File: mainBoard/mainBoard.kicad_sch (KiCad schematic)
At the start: 15 parts, among them J1 Conn_01x04, J2 Conn_01x04, J6 Conn_01x07, J7 Conn_01x07

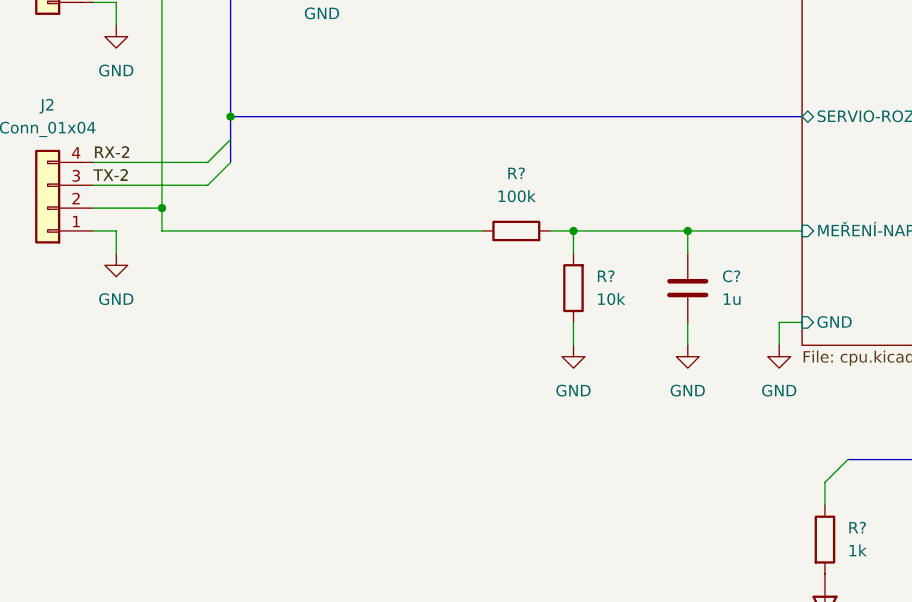
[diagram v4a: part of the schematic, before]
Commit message: test-point na děliči
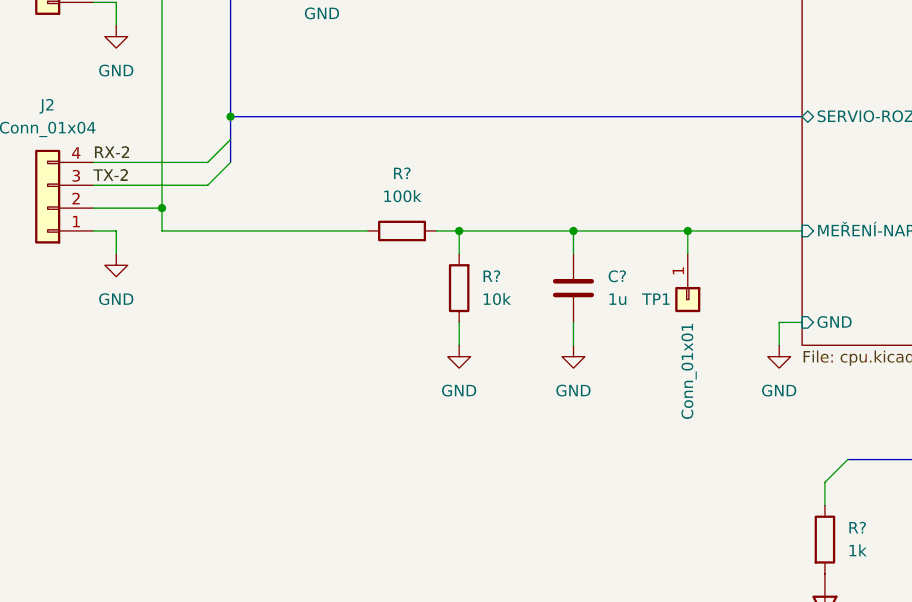
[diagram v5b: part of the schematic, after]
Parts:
- added TP1: Conn_01x01, Connector_Pin:Pin_D0.7mm_L6.5mm_W1.8mm_FlatFork, symbol Connector_Generic:Conn_01x01
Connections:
- net CPU/MEŘENÍ-NAPÁJENÍ: now also TP1.1 (Pin_1)
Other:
- moved on the sheet: C?, R?
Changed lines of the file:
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@@
   (junction (at 63.5 88.9) (diameter 0) (color 0 0 0 0)
   )
+  (junction (at 101.6 101.6) (diameter 0) (color 0 0 0 0)
+  )
   (junction (at 55.88 66.04) (diameter 0) (color 255 0 0 1)
   )
@@
   (junction (at 114.3 101.6) (diameter 0) (color 0 0 0 0)
   )
-  (junction (at 101.6 101.6) (diameter 0) (color 0 0 0 0)
+  (junction (at 88.9 101.6) (diameter 0) (color 0 0 0 0)
   )
   (bus_entry (at 60.96 93.98) (size 2.54 -2.54)
@@
     (stroke (width 0) (type default))
   )
-  (wire (pts (xy 114.3 101.6) (xy 127 101.6))
-    (stroke (width 0) (type default))
-  )
-  (wire (pts (xy 99.06 101.6) (xy 101.6 101.6))
+  (wire (pts (xy 86.36 101.6) (xy 88.9 101.6))
     (stroke (width 0) (type default))
   )
@@
     (stroke (width 0) (type default))
   )
+  (wire (pts (xy 114.3 101.6) (xy 114.3 104.14))
+    (stroke (width 0) (type default))
+  )
   (bus (pts (xy 203.2 38.1) (xy 203.2 60.96))
     (stroke (width 0) (type default))
@@
     (stroke (width 0) (type default))
   )
-  (wire (pts (xy 101.6 111.76) (xy 101.6 114.3))
+  (wire (pts (xy 88.9 111.76) (xy 88.9 114.3))
     (stroke (width 0) (type default))
   )
@@
     (stroke (width 0) (type default))
   )
-  (wire (pts (xy 101.6 101.6) (xy 101.6 104.14))
-    (stroke (width 0) (type default))
-  )
-  (wire (pts (xy 101.6 101.6) (xy 114.3 101.6))
+  (wire (pts (xy 88.9 101.6) (xy 88.9 104.14))
+    (stroke (width 0) (type default))
+  )
+  (wire (pts (xy 88.9 101.6) (xy 101.6 101.6))
     (stroke (width 0) (type default))
   )
@@
     (stroke (width 0) (type default))
   )
-  (wire (pts (xy 114.3 104.14) (xy 114.3 101.6))
+  (wire (pts (xy 101.6 104.14) (xy 101.6 101.6))
     (stroke (width 0) (type default))
   )
@@
     (stroke (width 0) (type default) (color 255 0 0 1))
   )
+  (wire (pts (xy 114.3 101.6) (xy 127 101.6))
+    (stroke (width 0) (type default))
+  )
   (bus (pts (xy 203.2 66.04) (xy 203.2 68.58))
     (stroke (width 0) (type default))
@@
   )
   (wire (pts (xy 48.26 96.52) (xy 60.96 96.52))
+    (stroke (width 0) (type default))
+  )
+  (wire (pts (xy 101.6 101.6) (xy 114.3 101.6))
     (stroke (width 0) (type default))
   )
@@
     (stroke (width 0) (type default))
   )
-  (wire (pts (xy 114.3 111.76) (xy 114.3 114.3))
+  (wire (pts (xy 101.6 111.76) (xy 101.6 114.3))
     (stroke (width 0) (type default))
   )
@@
     (stroke (width 0.3) (type default) (color 0 0 0 1))
   )
-  (wire (pts (xy 91.44 101.6) (xy 55.88 101.6))
+  (wire (pts (xy 78.74 101.6) (xy 55.88 101.6))
     (stroke (width 0) (type default) (color 255 0 0 1))
   )
@@
     )
   )
-  (symbol (lib_id "Device:R") (at 101.6 107.95 180) (unit 1)
-    (in_bom yes) (on_board yes) (dnp no) (fields_autoplaced)
-    (property "Reference" "R?" (at 104.14 106.68 0)
+  (symbol (lib_id "Device:R") (at 88.9 107.95 180) (unit 1)
+    (in_bom yes) (on_board yes) (dnp no) (fields_autoplaced)
+    (property "Reference" "R?" (at 91.44 106.68 0)
       (effects (font (size 1.27 1.27)) (justify right))
     )
-    (property "Value" "10k" (at 104.14 109.22 0)
+    (property "Value" "10k" (at 91.44 109.22 0)
       (effects (font (size 1.27 1.27)) (justify right))
     )
-    (property "Footprint" "Capacitor_SMD:C_0402_1005Metric" (at 103.378 107.95 90)
-      (effects (font (size 1.27 1.27)) hide)
-    )
-    (property "Datasheet" "~" (at 101.6 107.95 0)
-      (effects (font (size 1.27 1.27)) hide)
-    )
-    (property "LCSC" "C25744" (at 101.6 107.95 0)
+    (property "Footprint" "Capacitor_SMD:C_0402_1005Metric" (at 90.678 107.95 90)
+      (effects (font (size 1.27 1.27)) hide)
+    )
+    (property "Datasheet" "~" (at 88.9 107.95 0)
+      (effects (font (size 1.27 1.27)) hide)
+    )
+    (property "LCSC" "C25744" (at 88.9 107.95 0)
       (effects (font (size 1.27 1.27)) hide)
     )
@@
     )
   )
-  (symbol (lib_id "power:GND") (at 101.6 114.3 0) (unit 1)
-    (in_bom yes) (on_board yes) (dnp no) (fields_autoplaced)
-    (property "Reference" "#PWR04" (at 101.6 120.65 0)
-      (effects (font (size 1.27 1.27)) hide)
-    )
-    (property "Value" "GND" (at 101.6 119.38 0)
-      (effects (font (size 1.27 1.27)))
-    )
-    (property "Footprint" "" (at 101.6 114.3 0)
-      (effects (font (size 1.27 1.27)) hide)
-    )
-    (property "Datasheet" "" (at 101.6 114.3 0)
+  (symbol (lib_id "power:GND") (at 88.9 114.3 0) (unit 1)
+    (in_bom yes) (on_board yes) (dnp no) (fields_autoplaced)
+    (property "Reference" "#PWR04" (at 88.9 120.65 0)
+      (effects (font (size 1.27 1.27)) hide)
+    )
+    (property "Value" "GND" (at 88.9 119.38 0)
+      (effects (font (size 1.27 1.27)))
+    )
+    (property "Footprint" "" (at 88.9 114.3 0)
+      (effects (font (size 1.27 1.27)) hide)
+    )
+    (property "Datasheet" "" (at 88.9 114.3 0)
       (effects (font (size 1.27 1.27)) hide)
     )
@@
     )
   )
-  (symbol (lib_id "Device:R") (at 95.25 101.6 90) (unit 1)
-    (in_bom yes) (on_board yes) (dnp no) (fields_autoplaced)
-    (property "Reference" "R?" (at 95.25 95.25 90)
-      (effects (font (size 1.27 1.27)))
-    )
-    (property "Value" "100k" (at 95.25 97.79 90)
-      (effects (font (size 1.27 1.27)))
-    )
-    (property "Footprint" "Capacitor_SMD:C_0402_1005Metric" (at 95.25 103.378 90)
-      (effects (font (size 1.27 1.27)) hide)
-    )
-    (property "Datasheet" "~" (at 95.25 101.6 0)
-      (effects (font (size 1.27 1.27)) hide)
-    )
-    (property "LCSC" "C25741" (at 95.25 101.6 0)
+  (symbol (lib_id "Device:R") (at 82.55 101.6 90) (unit 1)
+    (in_bom yes) (on_board yes) (dnp no) (fields_autoplaced)
+    (property "Reference" "R?" (at 82.55 95.25 90)
+      (effects (font (size 1.27 1.27)))
+    )
+    (property "Value" "100k" (at 82.55 97.79 90)
+      (effects (font (size 1.27 1.27)))
+    )
+    (property "Footprint" "Capacitor_SMD:C_0402_1005Metric" (at 82.55 103.378 90)
+      (effects (font (size 1.27 1.27)) hide)
+    )
+    (property "Datasheet" "~" (at 82.55 101.6 0)
+      (effects (font (size 1.27 1.27)) hide)
+    )
+    (property "LCSC" "C25741" (at 82.55 101.6 0)
       (effects (font (size 1.27 1.27)) hide)
     )
@@
     )
   )
-  (symbol (lib_id "Device:C") (at 114.3 107.95 0) (unit 1)
+  (symbol (lib_id "Device:C") (at 101.6 107.95 0) (unit 1)
     (in_bom yes) (on_board yes) (dnp no)
-    (property "Reference" "C?" (at 118.11 106.68 0)
+    (property "Reference" "C?" (at 105.41 106.68 0)
       (effects (font (size 1.27 1.27)) (justify left))
     )
-    (property "Value" "1u" (at 118.11 109.22 0)
+    (property "Value" "1u" (at 105.41 109.22 0)
       (effects (font (size 1.27 1.27)) (justify left))
     )
-    (property "Footprint" "Capacitor_SMD:C_0402_1005Metric" (at 115.2652 111.76 0)
-      (effects (font (size 1.27 1.27)) hide)
-    )
-    (property "Datasheet" "~" (at 114.3 107.95 0)
-      (effects (font (size 1.27 1.27)) hide)
-    )
-    (property "LCSC" "C52923" (at 114.3 107.95 0)
+    (property "Footprint" "Capacitor_SMD:C_0402_1005Metric" (at 102.5652 111.76 0)
+      (effects (font (size 1.27 1.27)) hide)
+    )
+    (property "Datasheet" "~" (at 101.6 107.95 0)
+      (effects (font (size 1.27 1.27)) hide)
+    )
+    (property "LCSC" "C52923" (at 101.6 107.95 0)
       (effects (font (size 1.27 1.27)) hide)
     )
@@
     )
   )
-  (symbol (lib_id "power:GND") (at 114.3 114.3 0) (unit 1)
-    (in_bom yes) (on_board yes) (dnp no) (fields_autoplaced)
-    (property "Reference" "#PWR03" (at 114.3 120.65 0)
-      (effects (font (size 1.27 1.27)) hide)
-    )
-    (property "Value" "GND" (at 114.3 119.38 0)
-      (effects (font (size 1.27 1.27)))
-    )
-    (property "Footprint" "" (at 114.3 114.3 0)
-      (effects (font (size 1.27 1.27)) hide)
-    )
-    (property "Datasheet" "" (at 114.3 114.3 0)
+  (symbol (lib_id "power:GND") (at 101.6 114.3 0) (unit 1)
+    (in_bom yes) (on_board yes) (dnp no) (fields_autoplaced)
+    (property "Reference" "#PWR03" (at 101.6 120.65 0)
+      (effects (font (size 1.27 1.27)) hide)
+    )
+    (property "Value" "GND" (at 101.6 119.38 0)
+      (effects (font (size 1.27 1.27)))
+    )
+    (property "Footprint" "" (at 101.6 114.3 0)
+      (effects (font (size 1.27 1.27)) hide)
+    )
+    (property "Datasheet" "" (at 101.6 114.3 0)
       (effects (font (size 1.27 1.27)) hide)
     )
@@
         )
       )
+    )
+  )
+  (symbol (lib_id "Connector_Generic:Conn_01x01") (at 114.3 109.22 270) (unit 1)
+    (in_bom yes) (on_board yes) (dnp no)
+    (property "Reference" "TP1" (at 109.22 109.22 90)
+      (effects (font (size 1.27 1.27)) (justify left))
+    )
+    (property "Value" "Conn_01x01" (at 114.3 111.76 0)
+      (effects (font (size 1.27 1.27)) (justify left))
+    )
+    (property "Footprint" "Connector_Pin:Pin_D0.7mm_L6.5mm_W1.8mm_FlatFork" (at 114.3 109.22 0)
+      (effects (font (size 1.27 1.27)) hide)
+    )
+    (property "Datasheet" "~" (at 114.3 109.22 0)
+      (effects (font (size 1.27 1.27)) hide)
+    )
+    (pin "1")
+    (instances
+      (project "mainBoard"
+        (path "/30ed06d7-0b03-4878-b461-066cda7e7438/007b5876-baf1-4b85-a507-5fa12bfe2ac5"
+          (reference "TP1") (unit 1)
+        )
+        (path "/30ed06d7-0b03-4878-b461-066cda7e7438"
+          (reference "TP3") (unit 1)
+        )
+      )

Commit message: test-pointy na ENC-POT
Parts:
- added TP1: Conn_01x01, Connector_Pin:Pin_D0.7mm_L6.5mm_W1.8mm_FlatFork, symbol Connector_Generic:Conn_01x01
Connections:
- net ENC-POT: now also TP1.1 (Pin_1)
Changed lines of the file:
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@@
 (kicad_sch (version 20230121) (generator eeschema)
   (paper "A4")
+  (junction (at 214.63 25.4) (diameter 0) (color 0 0 0 0)
+  )
   (junction (at 55.88 73.66) (diameter 0) (color 255 0 0 1)
   )
@@
     (stroke (width 0) (type default) (color 255 0 0 1))
   )
+  (wire (pts (xy 214.63 25.4) (xy 224.79 25.4))
+    (stroke (width 0) (type default))
+  )
   (wire (pts (xy 73.66 69.85) (xy 76.2 69.85))
     (stroke (width 0.3) (type default) (color 0 0 0 1))
@@
     (stroke (width 0.3) (type default) (color 0 0 0 1))
   )
-  (wire (pts (xy 205.74 25.4) (xy 224.79 25.4))
+  (wire (pts (xy 205.74 25.4) (xy 214.63 25.4))
     (stroke (width 0) (type default))
   )
@@
     (stroke (width 0) (type default) (color 255 0 0 1))
   )
+  (wire (pts (xy 214.63 19.05) (xy 214.63 25.4))
+    (stroke (width 0) (type default))
+  )
   (bus (pts (xy 203.2 30.48) (xy 203.2 33.02))
     (stroke (width 0) (type default))
@@
   (wire (pts (xy 222.25 40.64) (xy 224.79 40.64))
     (stroke (width 0.3) (type default) (color 0 0 0 1))
+  )
+  (wire (pts (xy 214.63 19.05) (xy 224.79 19.05))
+    (stroke (width 0) (type default))
   )
   (wire (pts (xy 129.54 129.54) (xy 129.54 132.08))
@@
         )
       )
+    )
+  )
+  (symbol (lib_id "Connector_Generic:Conn_01x01") (at 229.87 19.05 0) (unit 1)
+    (in_bom yes) (on_board yes) (dnp no)
+    (property "Reference" "TP1" (at 228.6 15.24 0)
+      (effects (font (size 1.27 1.27)) (justify left))
+    )
+    (property "Value" "Conn_01x01" (at 232.41 19.05 0)
+      (effects (font (size 1.27 1.27)) (justify left))
+    )
+    (property "Footprint" "Connector_Pin:Pin_D0.7mm_L6.5mm_W1.8mm_FlatFork" (at 229.87 19.05 0)
+      (effects (font (size 1.27 1.27)) hide)
+    )
+    (property "Datasheet" "~" (at 229.87 19.05 0)
+      (effects (font (size 1.27 1.27)) hide)
+    )
+    (pin "1")
+    (instances
+      (project "mainBoard"
+        (path "/30ed06d7-0b03-4878-b461-066cda7e7438/007b5876-baf1-4b85-a507-5fa12bfe2ac5"
+          (reference "TP1") (unit 1)
+        )
+        (path "/30ed06d7-0b03-4878-b461-066cda7e7438"
+          (reference "TP4") (unit 1)
+        )
+      )

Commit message: WIP
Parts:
- removed R?: 1k, Capacitor_SMD:C_0402_1005Metric, symbol Device:R
- J7: footprint Connector_PinHeader_1.00mm:PinHeader_1x07_P1.00mm_Horizontal -> Connector_PinHeader_1.00mm:PinHeader_1x07_P1.00mm_Vertical
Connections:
- net GND: now also R?.2, R?.2; no longer D1.1 (K), D2.1 (K), D3.1 (K)
- net at D2.2 (A): no longer R?.2
- net at R?.1: now also D1.1 (K), D3.1 (K)
- net at D1.2 (A): no longer R?.2
- net at R?.1: now also D2.1 (K)
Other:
- note removed: "SERVIO-ROZHRANÍ"
- moved on the sheet: C?, D1, D2, D3, D4, J1, J2, J6, J7, R?, TP1

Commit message: WIP
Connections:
- net LED-B: now reaches D3.2 (A)
- net LED-Y: now reaches R?.1
- net LED-G: now reaches D2.2 (A)
- net LED-R: now reaches D1.2 (A)
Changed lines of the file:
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@@
   (junction (at 214.63 30.48) (diameter 0) (color 0 0 0 0)
+  )
+  (junction (at 55.88 91.44) (diameter 0) (color 255 0 0 1)
   )
   (junction (at 129.54 147.32) (diameter 0) (color 0 0 0 0)
@@
     (stroke (width 0) (type default))
   )
+  (wire (pts (xy 55.88 91.44) (xy 55.88 104.14))
+    (stroke (width 0) (type default) (color 255 0 0 1))
+  )
   (bus (pts (xy 63.5 88.9) (xy 63.5 96.52))
     (stroke (width 0) (type default))
@@
     (stroke (width 0.3) (type default) (color 0 0 0 1))
   )
-  (wire (pts (xy 55.88 81.28) (xy 55.88 104.14))
+  (wire (pts (xy 205.74 38.1) (xy 224.79 38.1))
+    (stroke (width 0) (type default))
+  )
+  (wire (pts (xy 129.54 147.32) (xy 129.54 144.78))
+    (stroke (width 0) (type default))
+  )
+  (wire (pts (xy 48.26 99.06) (xy 60.96 99.06))
+    (stroke (width 0) (type default))
+  )
+  (wire (pts (xy 55.88 81.28) (xy 55.88 91.44))
     (stroke (width 0) (type default) (color 255 0 0 1))
-  )
-  (wire (pts (xy 205.74 38.1) (xy 224.79 38.1))
-    (stroke (width 0) (type default))
-  )
-  (wire (pts (xy 129.54 147.32) (xy 129.54 144.78))
-    (stroke (width 0) (type default))
-  )
-  (wire (pts (xy 48.26 99.06) (xy 60.96 99.06))
-    (stroke (width 0) (type default))
-  )
-  (bus (pts (xy 177.8 106.68) (xy 190.5 106.68))
-    (stroke (width 0) (type default))
   )
   (wire (pts (xy 88.9 106.68) (xy 88.9 109.22))
@@
     (stroke (width 0) (type default))
   )
+  (bus (pts (xy 177.8 106.68) (xy 190.5 106.68))
+    (stroke (width 0) (type default))
+  )
   (bus (pts (xy 203.2 71.12) (xy 203.2 73.66))
     (stroke (width 0) (type default))
@@
     (stroke (width 0) (type default))
   )
+  (label "LED-Y" (at 175.26 137.16 0) (fields_autoplaced)
+    (effects (font (size 1.27 1.27)) (justify left bottom))
+  )
+  (label "LED-G" (at 160.02 137.16 0) (fields_autoplaced)
+    (effects (font (size 1.27 1.27)) (justify left bottom))
+  )
   (label "ENC-POT" (at 224.79 63.5 180) (fields_autoplaced)
     (effects (font (size 1.27 1.27)) (justify right bottom))
@@
     (effects (font (size 1.27 1.27)) (justify right bottom))
   )
+  (label "LED-R" (at 129.54 137.16 0) (fields_autoplaced)
+    (effects (font (size 1.27 1.27)) (justify left bottom))
+  )
   (label "ENC-TYP-DETEKCE" (at 224.79 66.04 180) (fields_autoplaced)
     (effects (font (size 1.27 1.27)) (justify right bottom))
@@
   )
   (label "RX-2" (at 48.26 99.06 0) (fields_autoplaced)
+    (effects (font (size 1.27 1.27)) (justify left bottom))
+  )
+  (label "LED-B" (at 144.78 137.16 0) (fields_autoplaced)
     (effects (font (size 1.27 1.27)) (justify left bottom))
   )
@@
     )
   )
+  (symbol (lib_id "power:GND") (at 35.56 86.36 0) (unit 1)
+    (in_bom yes) (on_board yes) (dnp no) (fields_autoplaced)
+    (property "Reference" "#PWR010" (at 35.56 92.71 0)
+      (effects (font (size 1.27 1.27)) hide)
+    )
+    (property "Value" "GND" (at 35.56 91.44 0)
+      (effects (font (size 1.27 1.27)))
+    )
+    (property "Footprint" "" (at 35.56 86.36 0)
+      (effects (font (size 1.27 1.27)) hide)
+    )
+    (property "Datasheet" "" (at 35.56 86.36 0)
+      (effects (font (size 1.27 1.27)) hide)
+    )
+    (pin "1")
+    (instances
+      (project "mainBoard"
+        (path "/30ed06d7-0b03-4878-b461-066cda7e7438"
+          (reference "#PWR010") (unit 1)
+        )
+      )
+    )
+  )
   (symbol (lib_id "power:GND") (at 124.46 119.38 0) (unit 1)
     (in_bom yes) (on_board yes) (dnp no) (fields_autoplaced)
@@
     )
   )
+  (symbol (lib_id "power:PWR_FLAG") (at 35.56 86.36 0) (unit 1)
+    (in_bom yes) (on_board yes) (dnp no)
+    (property "Reference" "#FLG01" (at 35.56 84.455 0)
+      (effects (font (size 1.27 1.27)) hide)
+    )
+    (property "Value" "PWR_FLAG" (at 30.48 82.55 0)
+      (effects (font (size 1.27 1.27)) (justify left))
+    )
+    (property "Footprint" "" (at 35.56 86.36 0)
+      (effects (font (size 1.27 1.27)) hide)
+    )
+    (property "Datasheet" "~" (at 35.56 86.36 0)
+      (effects (font (size 1.27 1.27)) hide)
+    )
+    (pin "1")
+    (instances
+      (project "mainBoard"
+        (path "/30ed06d7-0b03-4878-b461-066cda7e7438/64dbc0d3-4eed-460b-93d3-a846dd72318b"
+          (reference "#FLG01") (unit 1)
+        )
+        (path "/30ed06d7-0b03-4878-b461-066cda7e7438"
+          (reference "#FLG03") (unit 1)
+        )
+      )
+    )
+  )
   (symbol (lib_id "Device:R") (at 129.54 153.67 0) (unit 1)
     (in_bom yes) (on_board yes) (dnp no) (fields_autoplaced)
@@
         )
       )
+    )
+  )
+  (symbol (lib_id "power:PWR_FLAG") (at 55.88 91.44 270) (unit 1)
+    (in_bom yes) (on_board yes) (dnp no)
+    (property "Reference" "#FLG01" (at 57.785 91.44 0)
+      (effects (font (size 1.27 1.27)) hide)
+    )
+    (property "Value" "PWR_FLAG" (at 59.69 86.36 0)
+      (effects (font (size 1.27 1.27)) (justify left))
+    )
+    (property "Footprint" "" (at 55.88 91.44 0)
+      (effects (font (size 1.27 1.27)) hide)
+    )
+    (property "Datasheet" "~" (at 55.88 91.44 0)
+      (effects (font (size 1.27 1.27)) hide)
+    )
+    (pin "1")
+    (instances
+      (project "mainBoard"
+        (path "/30ed06d7-0b03-4878-b461-066cda7e7438/64dbc0d3-4eed-460b-93d3-a846dd72318b"
+          (reference "#FLG01") (unit 1)
+        )
+        (path "/30ed06d7-0b03-4878-b461-066cda7e7438"
+          (reference "#FLG02") (unit 1)
+        )
+      )
